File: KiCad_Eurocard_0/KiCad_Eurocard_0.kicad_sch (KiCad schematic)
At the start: 0 parts

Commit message: Added ERA-1SM component
Added symbol and footprint files for the ERA-1SM and linked them together.
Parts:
- added IC1: ERA-1SM+, KiCad:ERA1SM, symbol ERA-1SM+:ERA-1SM+
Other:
- title: (none) -> Eurocard Schematic
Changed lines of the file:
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@@
 	(generator_version "9.0")
 	(paper "A4")
+	(title_block
+		(title "Eurocard Schematic")
+		(date "2026-03-03")
+		(rev "V0.1")
+	)
+	(symbol
+		(lib_id "ERA-1SM+:ERA-1SM+")
+		(at 29.21 63.5 0)
+		(unit 1)
+		(exclude_from_sim no)
+		(in_bom yes)
+		(on_board yes)
+		(dnp no)
+		(fields_autoplaced yes)
+		(property "Reference" "IC1"
+			(at 60.96 57.0798 0)
+			(effects
+				(font
+					(size 1.27 1.27)
+				)
+			)
+		)
+		(property "Value" "ERA-1SM+"
+			(at 60.96 59.6198 0)
+			(effects
+				(font
+					(size 1.27 1.27)
+				)
+			)
+		)
+		(property "Footprint" "KiCad:ERA1SM"
+			(at 55.88 130.48 0)
+			(effects
+				(font
+					(size 1.27 1.27)
+				)
+				(justify left top)
+				(hide yes)
+			)
+		)
+		(property "Datasheet" "https://www.minicircuits.com/WebStore/dashboard.html?model=ERA-1SM%2B&srsltid=AfmBOopMJ6LGZDp162-GJ4DyJ5EbXofCns5kIKCboT9UIHU_AO_H4lBL"
+			(at 55.88 230.48 0)
+			(effects
+				(font
+					(size 1.27 1.27)
+				)
+				(justify left top)
+				(hide yes)
+			)
+		)
+		(property "Description" "RF Amplifier SMT Gain Block, DC - 8000 MHz, 50 ohms"
+			(at 29.21 63.5 0)
+			(effects
+				(font
+					(size 1.27 1.27)
+				)
+				(hide yes)
+			)
+		)
+		(property "Height" "1.52"
+			(at 55.88 430.48 0)
+			(effects
+				(font
+					(size 1.27 1.27)
+				)
+				(justify left top)
+				(hide yes)
+			)
+		)
+		(property "Manufacturer_Name" "Mini-Circuits"
+			(at 55.88 530.48 0)
+			(effects
+				(font
+					(size 1.27 1.27)
+				)
+				(justify left top)
+				(hide yes)
+			)
+		)
+		(property "Manufacturer_Part_Number" "ERA-1SM+"
+			(at 55.88 630.48 0)
+			(effects
+				(font
+					(size 1.27 1.27)
+				)
+				(justify left top)
+				(hide yes)
+			)
+		)
+		(property "Mouser Part Number" "139-ERA-1SM"
+			(at 55.88 730.48 0)
+			(effects
+				(font
+					(size 1.27 1.27)
+				)
+				(justify left top)
+				(hide yes)
+			)
+		)
+		(property "Mouser Price/Stock" "https://www.mouser.co.uk/ProductDetail/Mini-Circuits/ERA-1SM%2b?qs=xZ%2FP%252Ba9zWqbAX5z6Z5ocXQ%3D%3D"
+			(at 55.88 830.48 0)
+			(effects
+				(font
+					(size 1.27 1.27)
+				)
+				(justify left top)
+				(hide yes)
+			)
+		)
+		(property "Arrow Part Number" ""
+			(at 55.88 930.48 0)
+			(effects
+				(font
+					(size 1.27 1.27)
+				)
+				(justify left top)
+				(hide yes)
+			)
+		)
+		(property "Arrow Price/Stock" ""
+			(at 55.88 1030.48 0)
+			(effects
+				(font
+					(size 1.27 1.27)
+				)
+				(justify left top)
+				(hide yes)
+			)
+		)
+		(pin "2"
+		)
+		(pin "3"
+		)
+		(pin "1"
+		)
+		(pin "4"
+		)
+		(instances
+			(project ""
+				(path "/9cb3cf89-0e72-4eef-94e8-d924ebdf2eea"
+					(reference "IC1")
+					(unit 1)
+				)
+			)
+		)
+	)
 	(sheet_instances
 		(path "/"

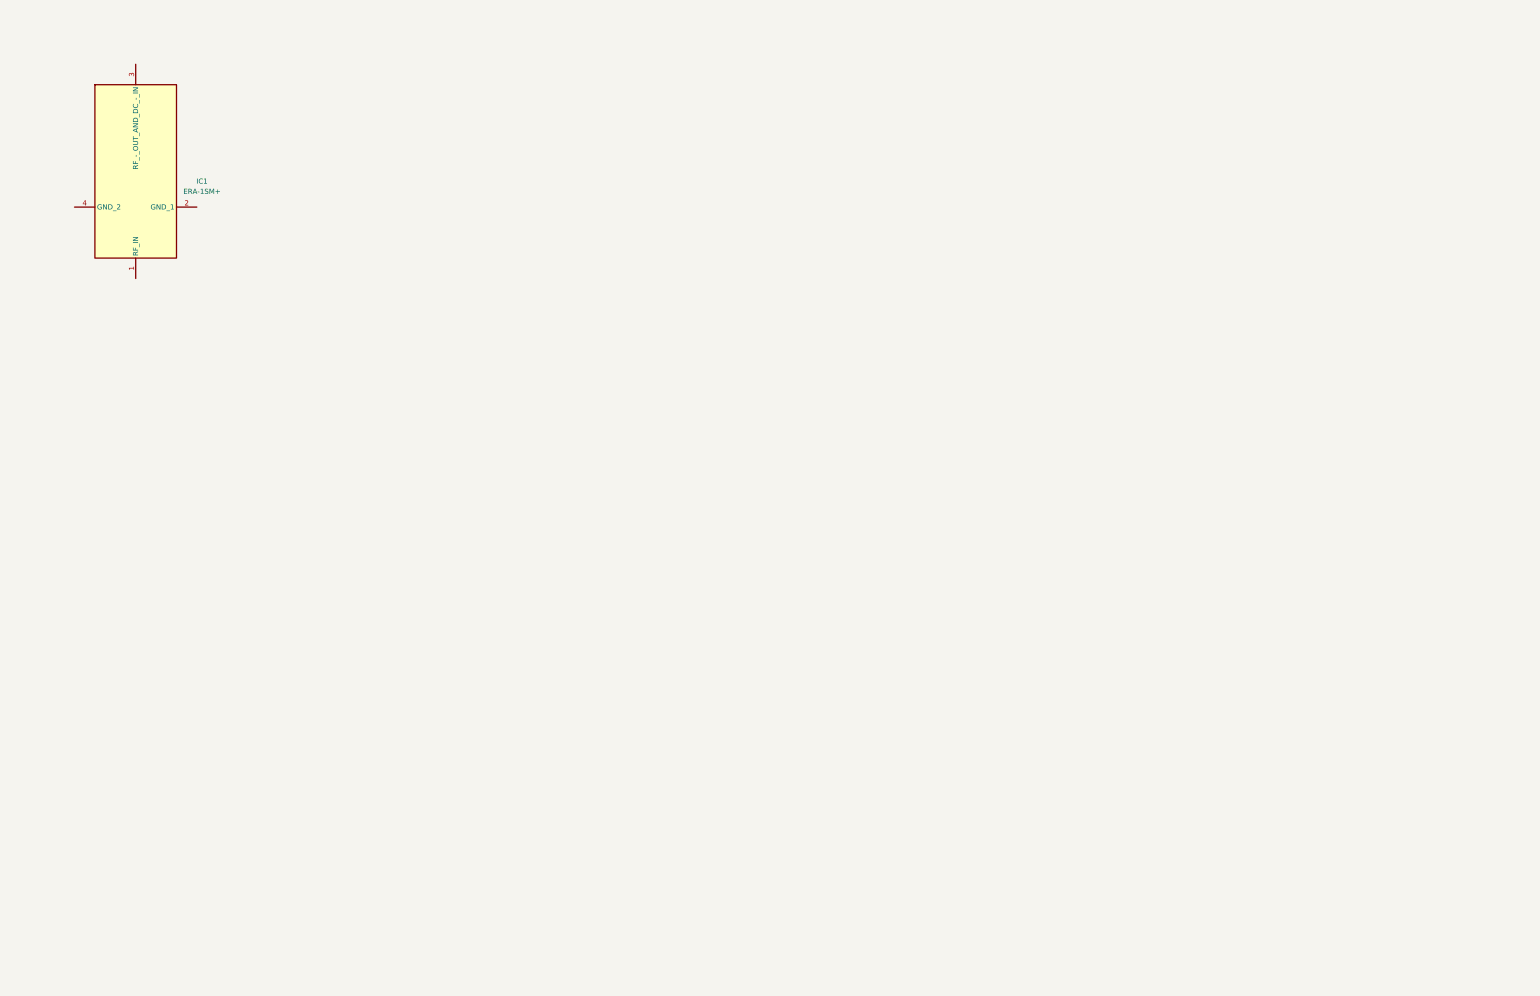
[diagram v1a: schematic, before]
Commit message: New Additions - Added new footprints
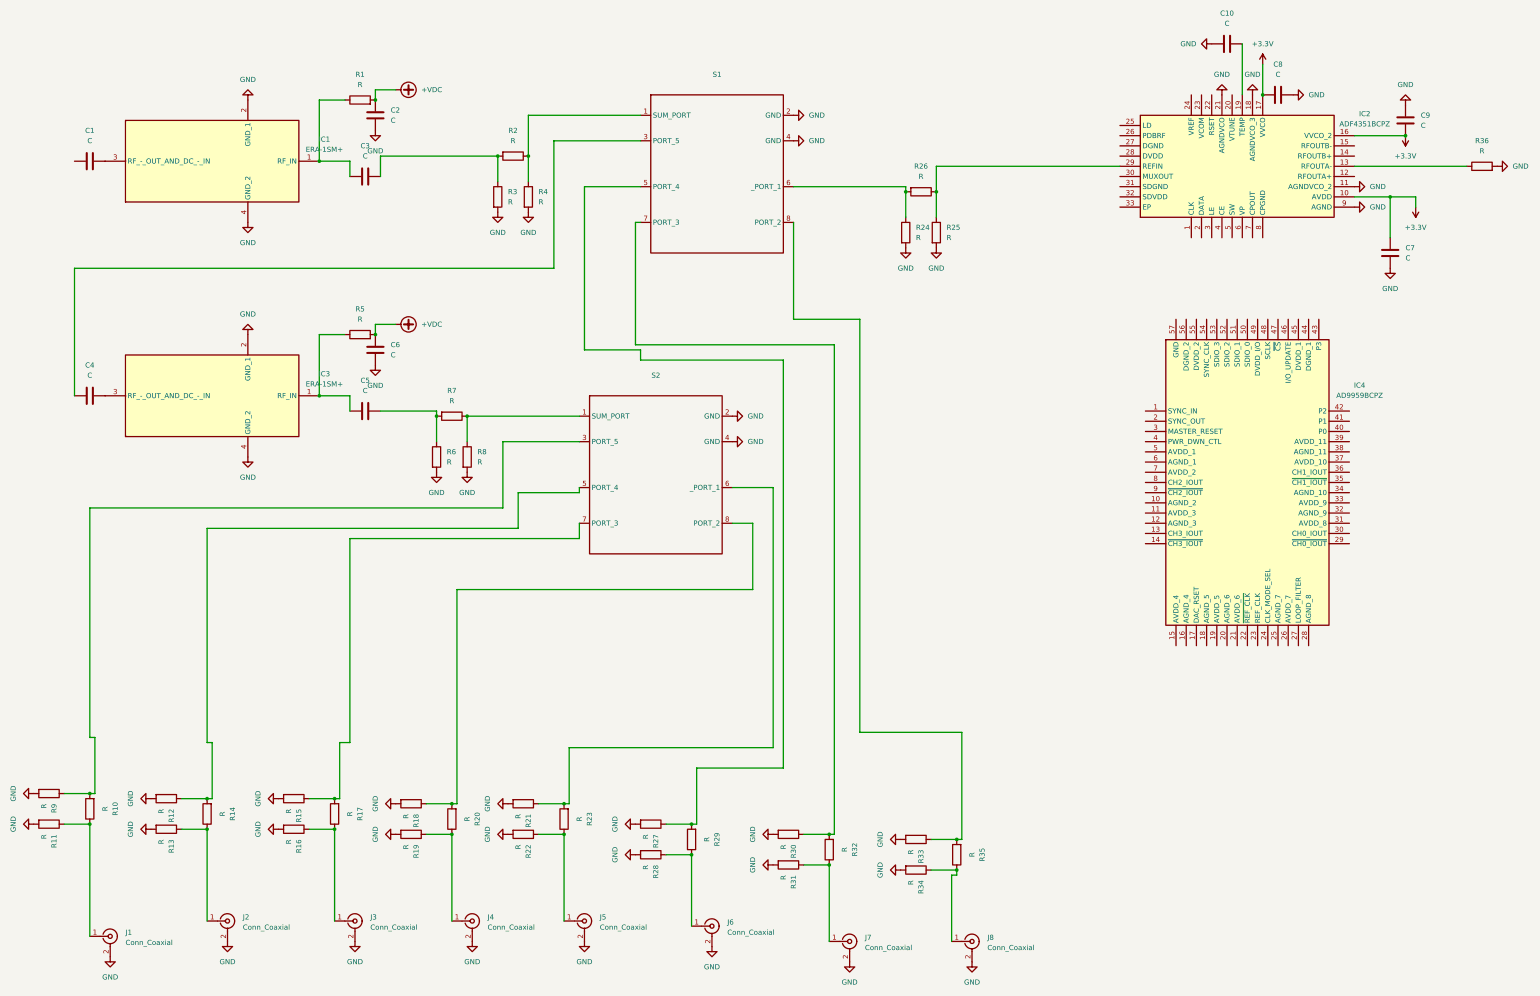
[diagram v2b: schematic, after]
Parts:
- added C1, C2, C3, C4, C5, C6: C, Capacitor_SMD:C_0402_1005Metric, symbol Device:C
- added C10, C7, C8, C9: C, symbol Device:C
- added IC2: ADF4351BCPZ, ADF4351BPCZ:QFN50P500X500X100-33N, symbol ADF4351BCPZ:ADF4351BCPZ
- added IC3: ERA-1SM+, ERA-1SM+:ERA1SM, symbol ERA-1SM+:ERA-1SM+
- added IC4: AD9959BCPZ, QFN50P800X800X100-57N-D, symbol AD9959BCPZ:AD9959BCPZ
- added J1, J2, J3, J4, J5, J6, J7, J8: Conn_Coaxial, symbol Connector:Conn_Coaxial
- added R1, R10, R11, R12, R13, R14, R15, R16, R17, R18, R19, R2, R20, R21, R22, R23, R24, R25, R26, R27, R28, R29, R3, R30, R31, R32, R33, R34, R35, R4, R5, R6, R7, R8, R9: R, Resistor_SMD:R_0402_1005Metric, symbol Device:R
- added R36: R, symbol Device:R
- added S1, S2: ~, symbol ERA-1SM+:SCP-5-1+
- IC1: footprint KiCad:ERA1SM -> ERA-1SM+:ERA1SM
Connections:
- net at IC1.1 (RF_IN): now also C3.2, R1.1
- net GND: now reaches IC1.2 (GND_1)
- net GND: now also IC1.4 (GND_2), C10.1, C2.1, C6.1, C7.1, C8.2, C9.1, IC2.11 (AGNDVCO_2), IC2.18 (AGNDVCO_3), IC2.21 (AGNDVCO), IC2.9 (AGND), IC3.2 (GND_1), IC3.4 (GND_2), J1.2 (Ext), J2.2 (Ext), J3.2 (Ext), J4.2 (Ext), J5.2 (Ext), J6.2 (Ext), J7.2 (Ext), J8.2 (Ext), R11.2, R12.2, R13.2, R15.2, R16.2, R18.2, R19.2, R21.2, R22.2, R24.2, R25.2, R27.2, R28.2, R3.2, R30.2, R31.2, R33.2, R34.2, R36.2, R4.2, R6.2, R8.2, R9.2, S1.2 (GND), S1.4 (GND), S2.2 (GND), S2.4 (GND)
- net at IC1.3 (RF_-_OUT_AND_DC_-_IN): now also C1.1
- new net: R15.1, R17.2, S2.7 (PORT_3)
- new net: J3.1 (In), R16.1, R17.1
- new net: J8.1 (In), R34.1, R35.1
- new net: J7.1 (In), R31.1, R32.1
- new net: R30.1, R32.2, S1.7 (PORT_3)
- new net: R18.1, R20.2, S2.8 (PORT_2)
- new net: J6.1 (In), R28.1, R29.1
- new net: R10.2, R9.1, S2.3 (PORT_5)
- new net: R24.1, R26.2, S1.6 (_PORT_1)
- new net: IC2.29 (REFIN), R25.1, R26.1
- new net: C5.1, R6.1, R7.2
- new net: J1.1 (In), R10.1, R11.1
- new net: C3.1, R2.2, R3.1
- new net: R2.1, R4.1, S1.1 (SUM_PORT)
- new net: C4.1, IC3.3 (RF_-_OUT_AND_DC_-_IN)
- new net: C4.2, S1.3 (PORT_5)
- new net: J5.1 (In), R22.1, R23.1
- new net: R7.1, R8.1, S2.1 (SUM_PORT)
- new net: J4.1 (In), R19.1, R20.1
- new net: C5.2, IC3.1 (RF_IN), R5.1
- new net: J2.1 (In), R13.1, R14.1
- new net: R12.1, R14.2, S2.5 (PORT_4)
- new net: R27.1, R29.2, S1.5 (PORT_4)
- new net: IC2.13 (RFOUTA-), R36.1
- new net: R21.1, R23.2, S2.6 (_PORT_1)
- new net: C10.2, IC2.19 (TEMP)
- new net: R33.1, R35.2, S1.8 (PORT_2)
- new net +3.3V: C7.2, C8.1, C9.2, IC2.10 (AVDD), IC2.16 (VVCO_2), IC2.17 (VVCO)
- new net +VDC: C2.2, C6.2, R1.2, R5.2
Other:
- moved on the sheet: IC1

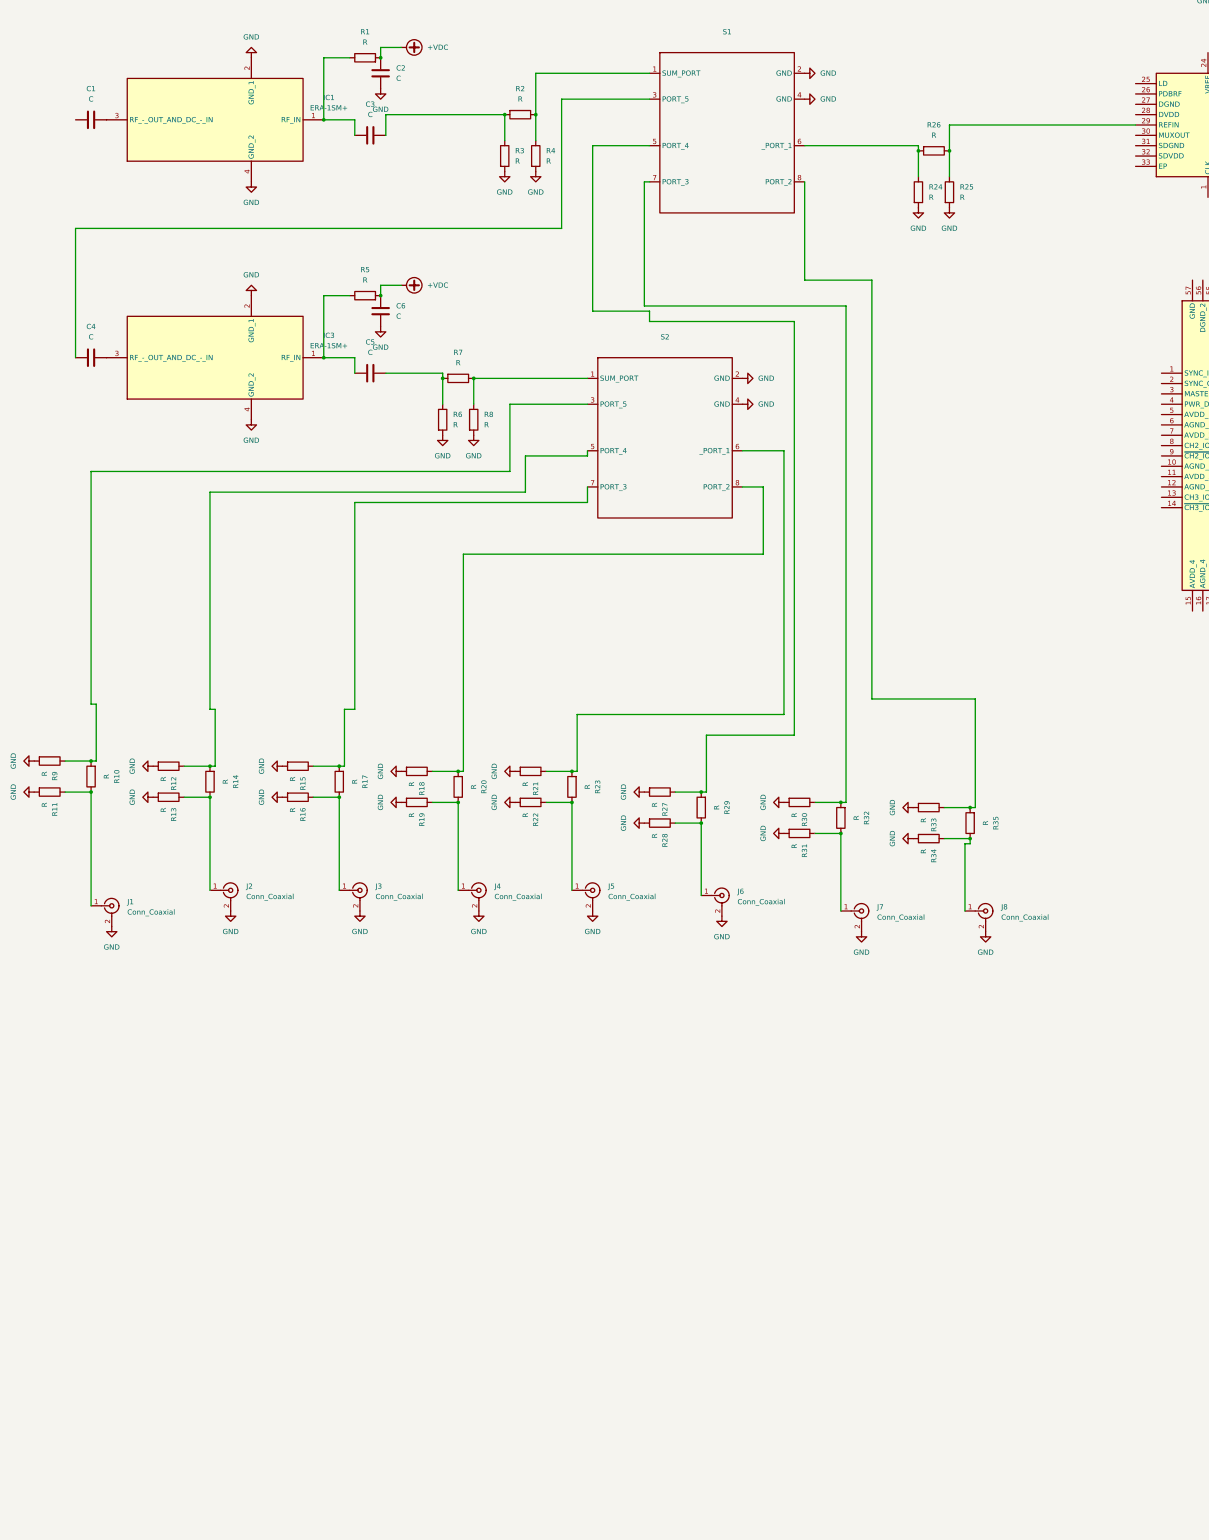
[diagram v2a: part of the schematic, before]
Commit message: Changed wires to gobal nets
still need to figure out DDS and ADF4351
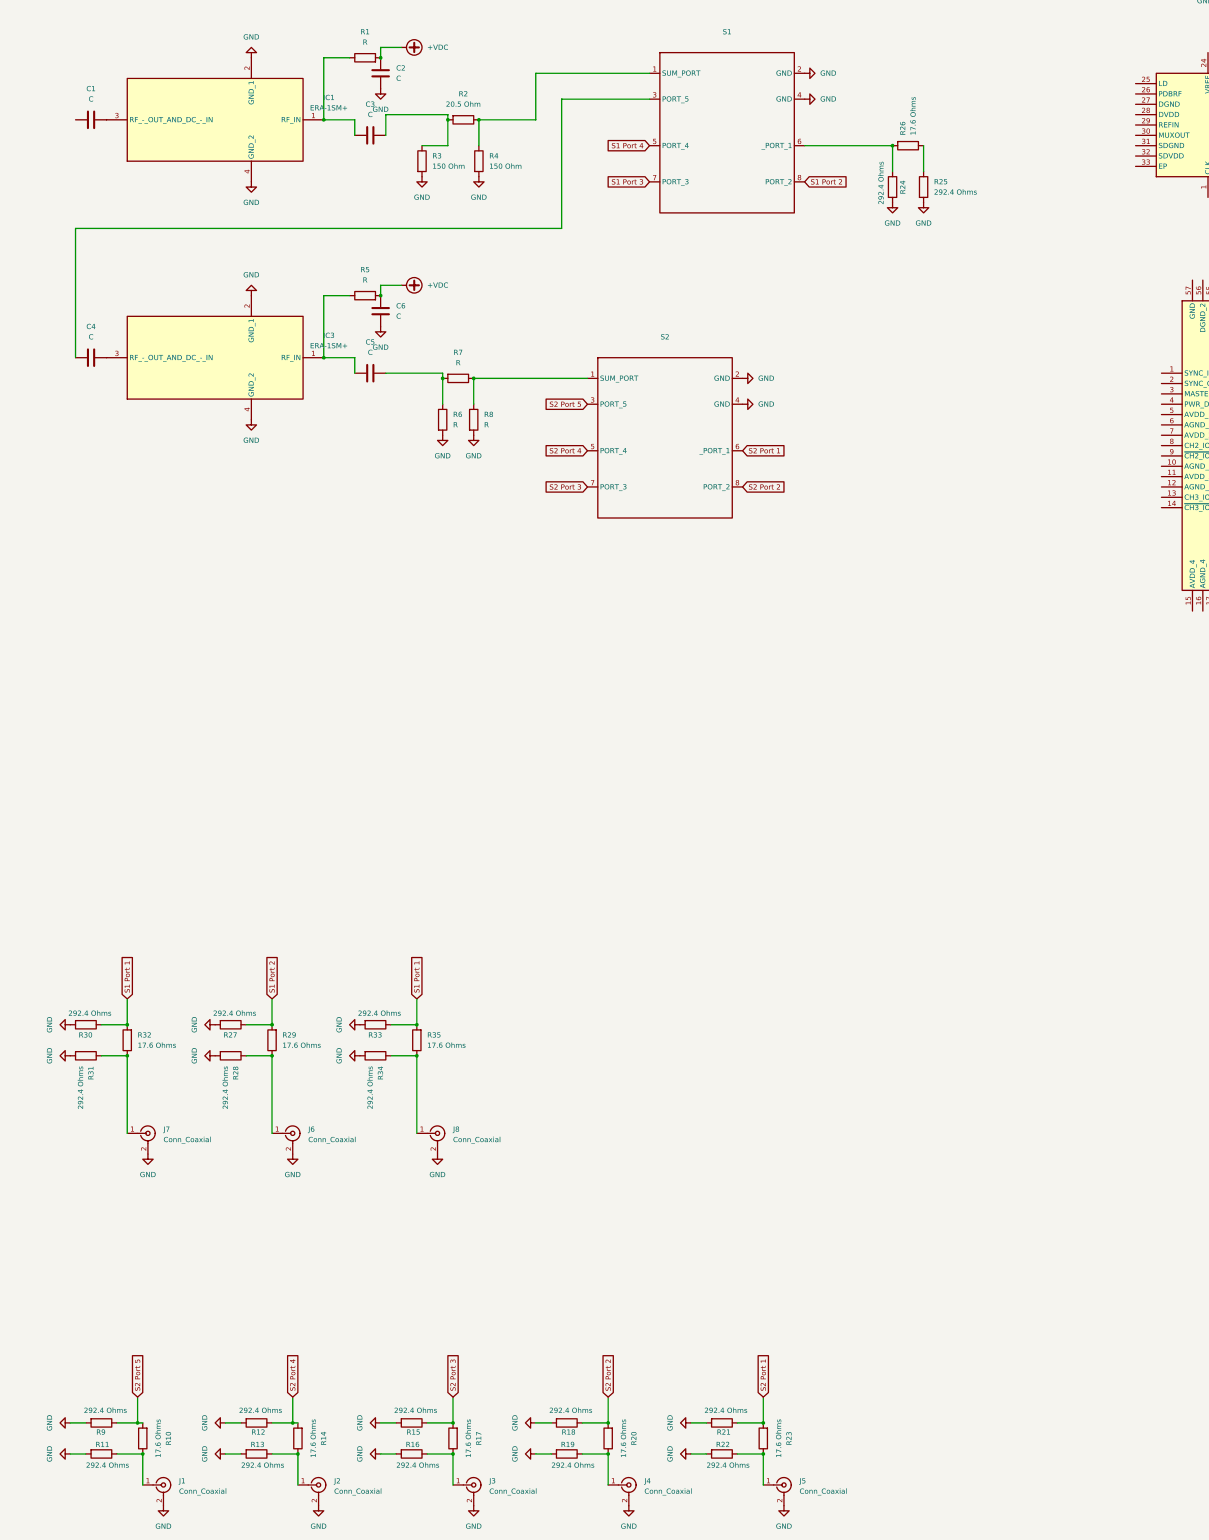
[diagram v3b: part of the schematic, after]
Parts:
- R10, R14, R17, R20, R23, R26, R29, R32, R35: value R -> 17.6 Ohms
- R11, R12, R13, R15, R16, R18, R19, R21, R22, R24, R25, R27, R28, R30, R31, R33, R34, R9: value R -> 292.4 Ohms
- R2: value R -> 20.5 Ohm
- R3, R4: value R -> 150 Ohm
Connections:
- net S2 Port 3: now reaches R15.1, R17.2, S2.7 (PORT_3)
- net S1 Port 1: now reaches R30.1, R32.2
- net S1 Port 1: now also R33.1, R35.2; no longer S1.7 (PORT_3)
- net S2 Port 2: now reaches R18.1, R20.2, S2.8 (PORT_2)
- net S2 Port 5: now reaches R10.2, R9.1, S2.3 (PORT_5)
- net at R25.1, R26.1: no longer IC2.29 (REFIN)
- net S2 Port 4: now reaches R12.1, R14.2, S2.5 (PORT_4)
- net S1 Port 2: now reaches R27.1, R29.2
- net S1 Port 2: now also S1.8 (PORT_2); no longer S1.5 (PORT_4)
- net S2 Port 1: now reaches R21.1, R23.2, S2.6 (_PORT_1)
- new net S1 Port 3: S1.7 (PORT_3)
- new net S1 Port 4: S1.5 (PORT_4)
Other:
- moved on the sheet: J1, J7, R10, R11, R2, R3, R30, R31, R32, R4, R9

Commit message: whoops forget to save
whoops
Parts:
- added C11: 10 pF, symbol Device:C
- added IC5: ADF4351BCPZ, ADF4351BPCZ:QFN50P500X500X100-33N, symbol ADF4351BCPZ:ADF4351BCPZ
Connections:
- net GND: now also IC5.27 (DGND), IC5.9 (AGND)
- new net: C11.1, IC5.29 (REFIN)
- new net 3.3V: IC5.10 (AVDD), IC5.17 (VVCO), IC5.28 (DVDD), IC5.32 (SDVDD), IC5.6 (VP)
